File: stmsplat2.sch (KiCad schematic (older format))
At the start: 112 parts, among them J1 C11_2X36, J10 Conn_01x03_Male, J11 Conn_01x02_Male, J12 Conn_01x04_Male, J13 Conn_01x04_Male, J14 Conn_01x02, J15 Conn_01x02, J16 Screw_Terminal_01x03, J17 Screw_Terminal_01x02, J2 C12_2X36, J3 Conn_01x04_Male, J4 Conn_01x04_Male, J5 Conn_Coaxial, J6 Conn_01x04_Male, J7 Conn_01x04_Male, J8 Conn_01x04_Male, J9 Conn_01x03_Male, Q1 BSS138LT1G, U1 ublox_chinese_PCB_module, U10 XCVR_E30-400M20S (Si4463), U11 3115_module, U2 ESP-C3-13U, U3 SST25VF032B, U4 48L512-48LM01, U5 Opamp_Quad_MCP6024, U6 E180-ZG120A, U7 AZ1084C, U8 MCP6S93-X_UN, U9 DS2485

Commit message: better placement, more handrouting, re-done power area etc
A few more passive comps added including dil switch
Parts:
- removed C24: 0.1uF, Capacitor_SMD:C_0805_2012Metric_Pad1.15x1.40mm_HandSolder, symbol Device:C
- removed TP5: TestPoint, TestPoint:TestPoint_Loop_D1.80mm_Drill1.0mm_Beaded, symbol Connector:TestPoint
- added C24: 10uF, Capacitor_SMD:CP_Elec_5x5.4, symbol Device:CP
- added C31: 100uF, Capacitor_SMD:CP_Elec_6.3x7.7, symbol Device:CP
- added J18, J19: Conn_01x02_Male, Connector_PinHeader_2.54mm:PinHeader_1x02_P2.54mm_Vertical, symbol Connector:Conn_01x02_Male
- added SW1: SW_DIP_x02, Button_Switch_SMD:SW_DIP_SPSTx02_Slide_Omron_A6S-210x_W8.9mm_P2.54mm, symbol Switch:SW_DIP_x02
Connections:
- net GND: now also C24.2, C31.2, J18.2 (Pin_2), SW1.3, SW1.4
- net NRST: now also J18.1 (Pin_1)
- net PD2: now also SW1.1
- net PD7: now also SW1.2
- net RAW5V: now also J16.1 (Pin_1); no longer J16.3 (Pin_3)
- net RAWGND: now also J16.3 (Pin_3); no longer J16.1 (Pin_1)
- net VDD: now also C31.1, J19.2 (Pin_2); no longer C13.1, J16.2 (Pin_2), U7.2 (VO)
- new net: C13.1, C24.1, J16.2 (Pin_2), J19.1 (Pin_1), U7.2 (VO)
- no-connect marks 75 -> 72
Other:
- note added: "EBAY MINIATURE\nNEO7M MODULE (NO ANTENNA)\nMODULE SMA CONN"
- note added: "EXT PWR\nJMPR"
- note added: "PIN3 +3V3 OUTPUT\nPIN2 +5V PSU INPUT\nPIN1 GROUND"
- note added: "RESET HEADER"
- note added: "VER 0.16\nADDED RESET HEADER + DIL SWITXH\nPOWERCONN SIGNALS"
- note removed: "EBAY MINATURE\nNEO7M MODULE (NO ANTENNA)\nMODULE SMA CONN"
- note removed: "PIN3 +5V PSU INPUT\nPIN2 +3V3 OUTPUT\nPIN1 GROUND"
- note removed: "VER 0.13: FROZEN \nSPI2<->SPI3 SWAPPED"
- moved on the sheet: C13, C15, C20, C25, FB1, J16, TP2, TP3, U1, U7

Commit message: PCB Layout finished. Gerbers produced, needs checking
Ready to send off to PCB house?
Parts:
- R5, R6: footprint Resistor_SMD:R_2010_5025Metric_Pad1.52x2.65mm_HandSolder -> Resistor_SMD:R_0805_2012Metric
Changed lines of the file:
@@
 F 0 "R6" H 9970 2346 50  0000 L CNN
 F 1 "100R" H 9970 2255 50  0000 L CNN
-F 2 "Resistor_SMD:R_2010_5025Metric_Pad1.52x2.65mm_HandSolder" V 9830 2300 50  0001 C CNN
+F 2 "Resistor_SMD:R_0805_2012Metric" V 9830 2300 50  0001 C CNN
 F 3 "~" H 9900 2300 50  0001 C CNN
 	1    9900 2300
@@
 F 0 "R5" H 9970 1796 50  0000 L CNN
 F 1 "100R" H 9970 1705 50  0000 L CNN
-F 2 "Resistor_SMD:R_2010_5025Metric_Pad1.52x2.65mm_HandSolder" V 9830 1750 50  0001 C CNN
+F 2 "Resistor_SMD:R_0805_2012Metric" V 9830 1750 50  0001 C CNN
 F 3 "~" H 9900 1750 50  0001 C CNN
 	1    9900 1750
@@
 PIN3 +3V3 OUTPUT\nPIN2 +5V PSU INPUT\nPIN1 GROUND
 Wire Wire Line
-	10300 7650 10750 7650
+	10300 7650 10550 7650
 $Comp
 L Connector:Conn_01x04_Male J13
@@
 	9800 7650 9800 7750
 Connection ~ 9800 7750
+$Comp
+L power:PWR_FLAG #FLG0102
+U 1 1 61B0F565
+P 10550 7650
+F 0 "#FLG0102" H 10550 7725 50  0001 C CNN
+F 1 "PWR_FLAG" H 10650 7800 50  0000 C CNN
+F 2 "" H 10550 7650 50  0001 C CNN
+F 3 "~" H 10550 7650 50  0001 C CNN
+	1    10550 7650
+	1    0    0    -1
+$EndComp
+Connection ~ 10550 7650
+Wire Wire Line
+	10550 7650 10750 7650
 $EndSCHEMATC

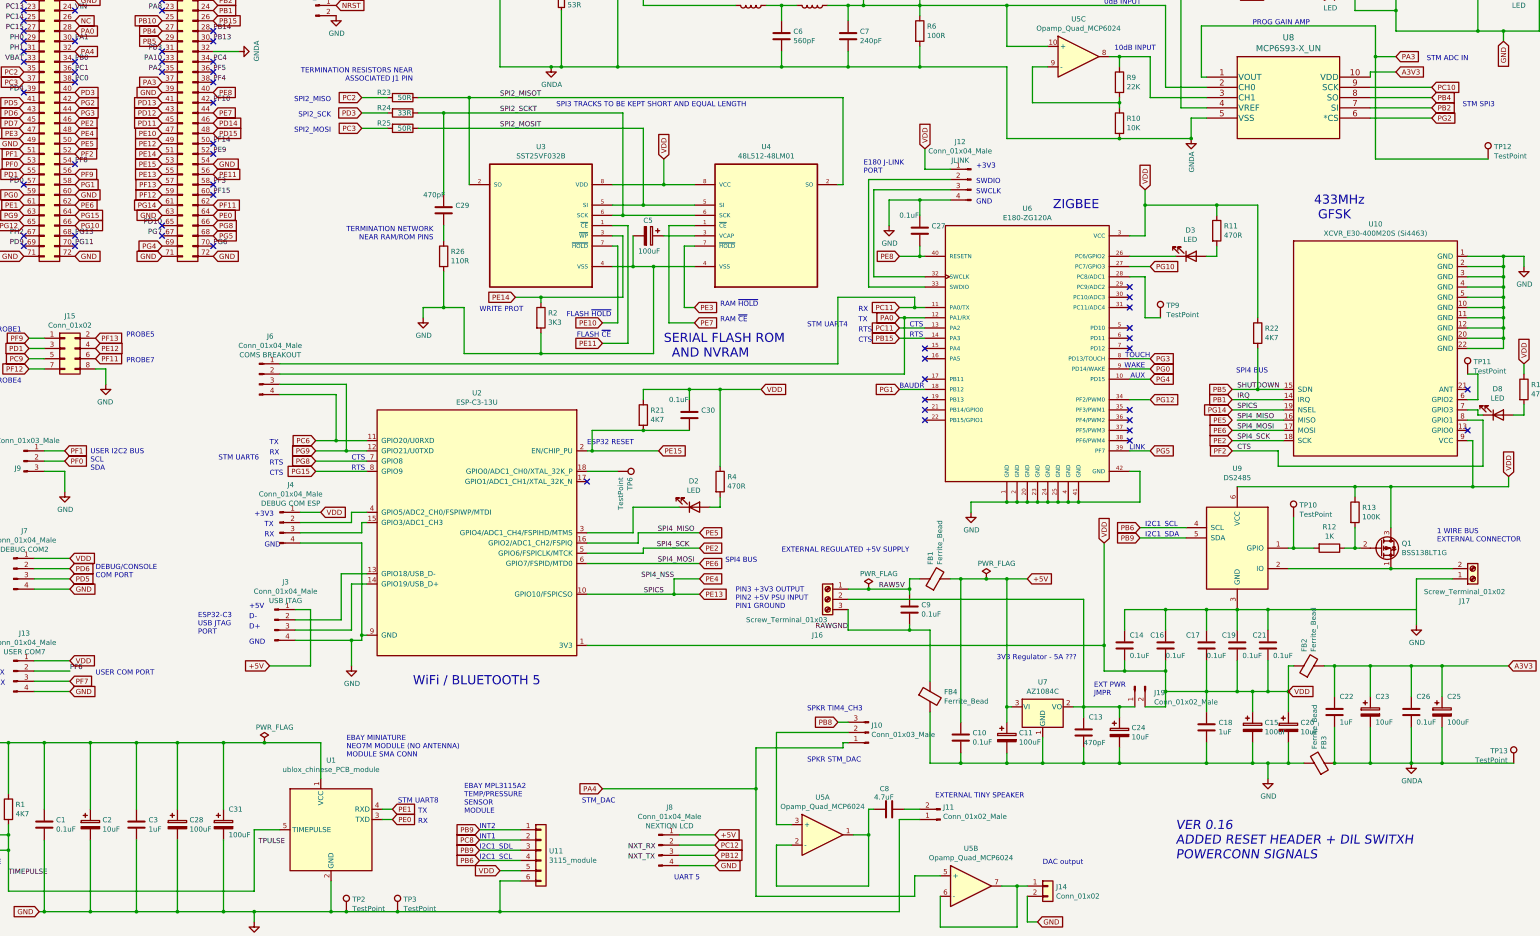
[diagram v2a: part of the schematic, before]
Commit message: U8 pads adjustment. PC0->GND, minor silkscreen tweaks
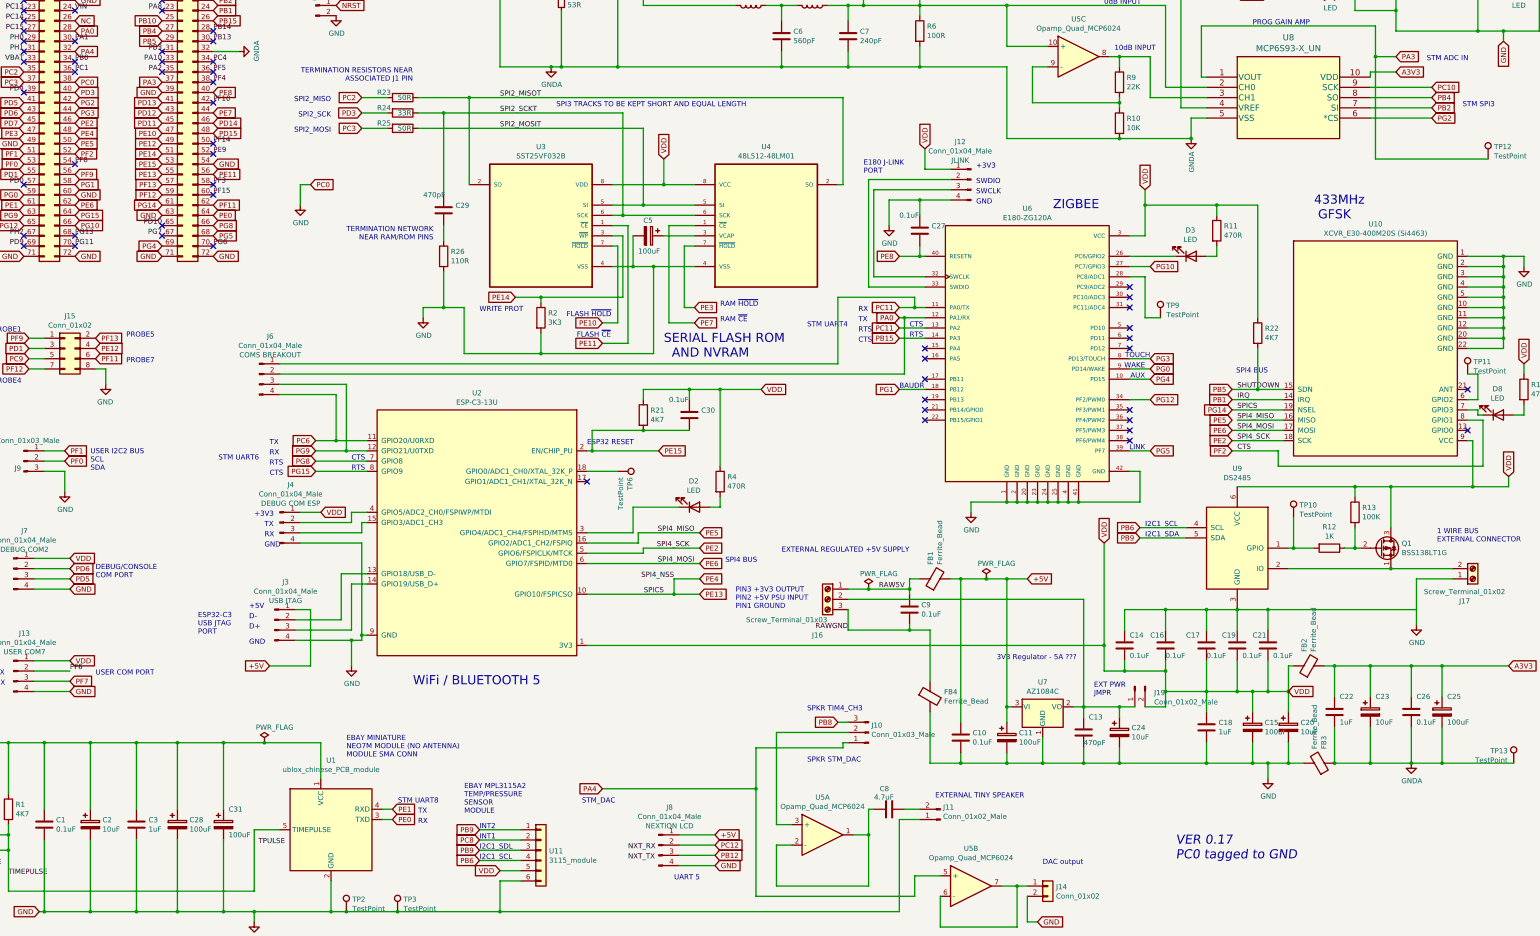
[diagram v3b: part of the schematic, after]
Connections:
- net PC0 is gone; now on net GND: J1.38 (Pin_38)
- no-connect marks 72 -> 71
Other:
- note added: "VER 0.17\nPC0 tagged to GND"
- note removed: "VER 0.16\nADDED RESET HEADER + DIL SWITXH\nPOWERCONN SIGNALS"
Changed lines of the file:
@@
 Text Label 1650 2700 0    50   ~ 0
 PC1
-Text Label 1650 2800 0    50   ~ 0
-PC0
 Text GLabel 1650 2900 2    50   Input ~ 0
 PD3
@@
 SERIAL FLASH ROM\n  AND NVRAM
 Text Notes 12400 10400 0    89   Italic 0
-VER 0.16\nADDED RESET HEADER + DIL SWITXH\nPOWERCONN SIGNALS
+VER 0.17\nPC0 tagged to GND
 $Comp
 L Connector_Generic:Conn_01x02 J14
@@
 NoConn ~ 1650 2600
 NoConn ~ 1650 2700
-NoConn ~ 1650 2800
 NoConn ~ 1150 2900
 NoConn ~ 1150 3800
@@
 Wire Wire Line
 	10550 7650 10750 7650
+Text GLabel 1650 2800 2    50   Input ~ 0
+PC0
+Text GLabel 3950 3800 2    50   Input ~ 0
+PC0
+$Comp
+L power:GND #PWR0102
+U 1 1 61B4DC3D
+P 3850 4000
+F 0 "#PWR0102" H 3850 3750 50  0001 C CNN
+F 1 "GND" H 3855 3827 50  0000 C CNN
+F 2 "" H 3850 4000 50  0001 C CNN
+F 3 "" H 3850 4000 50  0001 C CNN
+	1    3850 4000
+	1    0    0    -1
+$EndComp
+Wire Wire Line
+	3950 3800 3850 3800
+Wire Wire Line
+	3850 3800 3850 4000
 $EndSCHEMATC

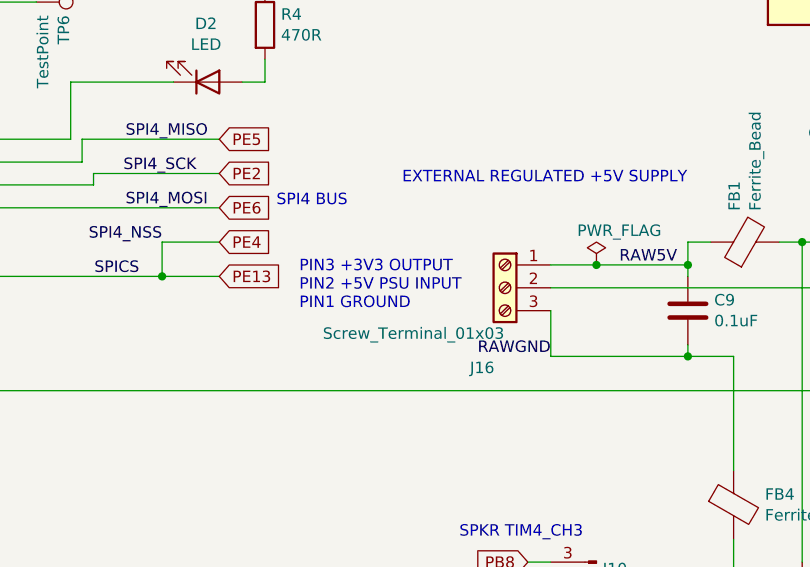
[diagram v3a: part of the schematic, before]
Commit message: Correct the PowerConn Pin assignments
these were changed to facilitate easier PCB layout
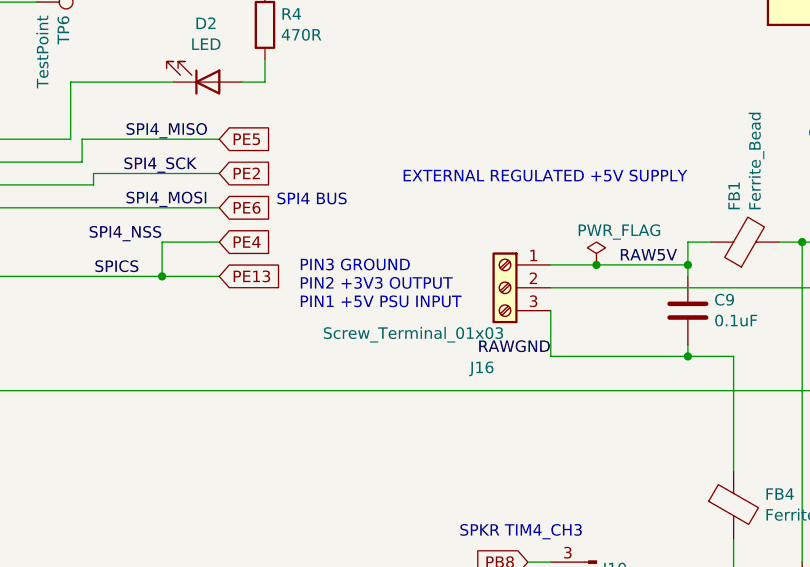
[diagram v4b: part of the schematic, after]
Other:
- note added: "PIN3 GROUND\nPIN2 +3V3 OUTPUT\nPIN1 +5V PSU INPUT"
- note removed: "PIN3 +3V3 OUTPUT\nPIN2 +5V PSU INPUT\nPIN1 GROUND"
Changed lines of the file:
@@
 $EndComp
 Text Notes 8100 7950 0    50   ~ 0
-PIN3 +3V3 OUTPUT\nPIN2 +5V PSU INPUT\nPIN1 GROUND
+PIN3 GROUND\nPIN2 +3V3 OUTPUT\nPIN1 +5V PSU INPUT
 Wire Wire Line
 	10300 7650 10550 7650

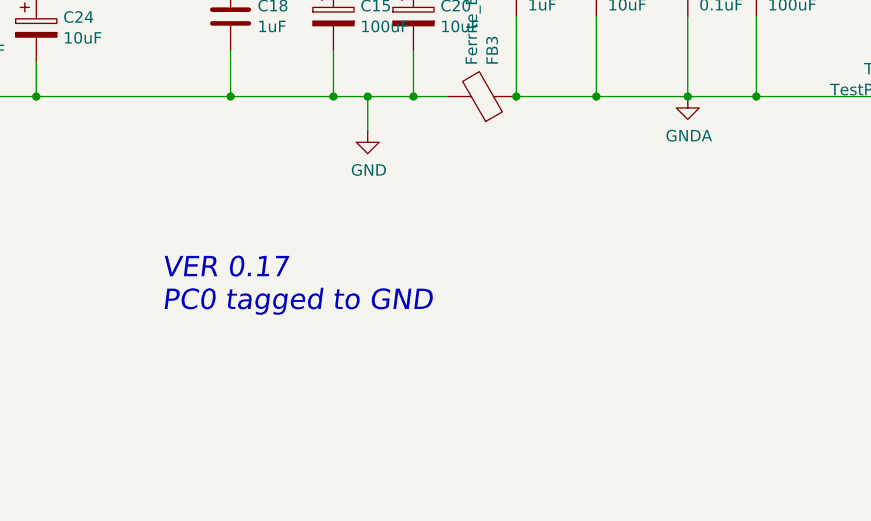
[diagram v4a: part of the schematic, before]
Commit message: Forgot to bump Schematic version
This is now bumped to Ver 0.18
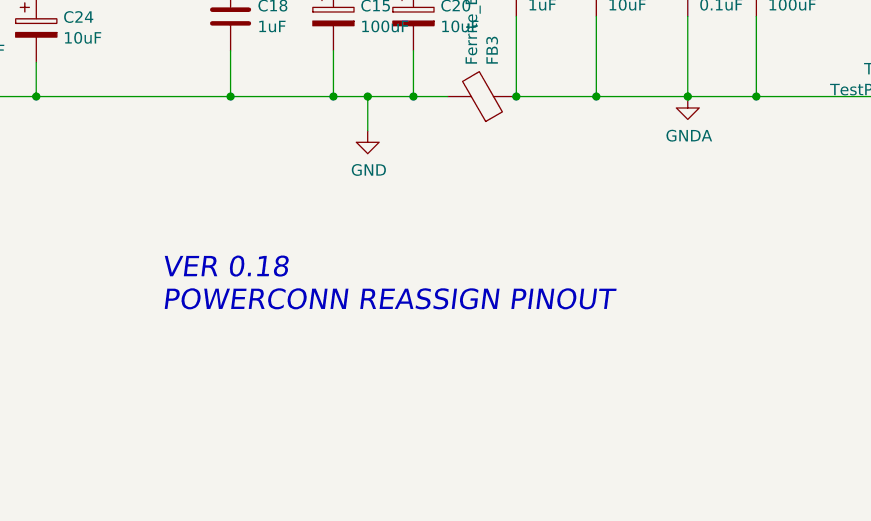
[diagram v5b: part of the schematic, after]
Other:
- note added: "VER 0.18\nPOWERCONN REASSIGN PINOUT"
- note removed: "VER 0.17\nPC0 tagged to GND"
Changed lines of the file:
@@
 SERIAL FLASH ROM\n  AND NVRAM
 Text Notes 12400 10400 0    89   Italic 0
-VER 0.17\nPC0 tagged to GND
+VER 0.18\nPOWERCONN REASSIGN PINOUT
 $Comp
 L Connector_Generic:Conn_01x02 J14
